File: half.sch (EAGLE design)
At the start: 112 parts, among them IC1 TLC59711, IC2 TLC59711, IC3 TLC59711, IC4 74HC08D, J2 AUDIO_JACK_TRRSCUI, J3 AUDIO_JACK_TRRSCUI, J4 FEMALE 2x3, J5 FEMALE 2x3, SW11 CHERRY-MX-LEDSMD, SW12 CHERRY-MX-LEDSMD, SW13 CHERRY-MX-LEDSMD, SW14 CHERRY-MX-LEDSMD, SW15 CHERRY-MX-LEDSMD, SW16 CHERRY-MX-LEDSMD, SW21 CHERRY-MX-LEDSMD, SW22 CHERRY-MX-LEDSMD, SW23 CHERRY-MX-LEDSMD, SW24 CHERRY-MX-LEDSMD, SW25 CHERRY-MX-LEDSMD, SW26 CHERRY-MX-LEDSMD, SW31 CHERRY-MX-LEDSMD, SW32 CHERRY-MX-LEDSMD, SW33 CHERRY-MX-LEDSMD, SW34 CHERRY-MX-LEDSMD, SW35 CHERRY-MX-LEDSMD, SW36 CHERRY-MX-LEDSMD, SW41 CHERRY-MX-LEDSMD, SW42 CHERRY-MX-LEDSMD, SW43 CHERRY-MX-LEDSMD, SW44 CHERRY-MX-LEDSMD, SW45 CHERRY-MX-LEDSMD, SW46 CHERRY-MX-LEDSMD, SW51 CHERRY-MX-LEDSMD, SW52 CHERRY-MX-LEDSMD, SW53 CHERRY-MX-LEDSMD, SW54 CHERRY-MX-LEDSMD, SW55 CHERRY-MX-LEDSMD, SW56 CHERRY-MX-LEDSMD, U1 MBT40, U2 SPX3819-3.3, U3 MCP73831T-2ACI/OT, U4 32U4, Y1 8MHz

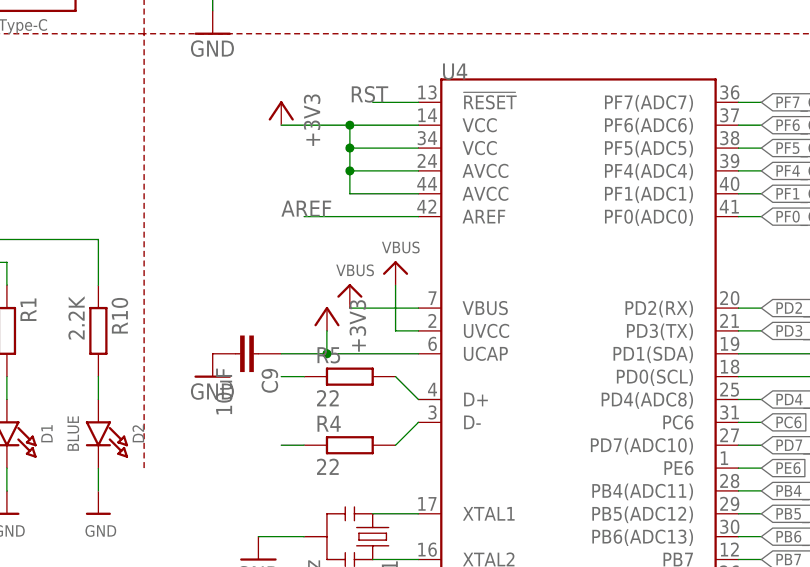
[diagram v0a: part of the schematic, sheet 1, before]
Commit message: Disconnect UVCC on 32u4 to reflect a greenwire fix on PCB
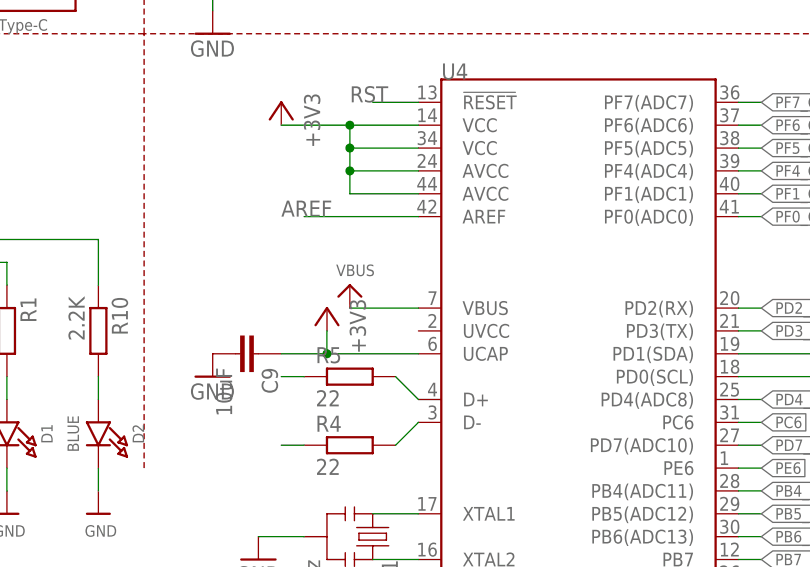
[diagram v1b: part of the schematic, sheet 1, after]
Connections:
- net VBUS: no longer U4.UVCC
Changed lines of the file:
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@@
 <part name="+3V5" library="supply1" deviceset="+3V3" device=""/>
 <part name="U$59" library="microbuilder" deviceset="VBUS" device=""/>
-<part name="U$60" library="microbuilder" deviceset="VBUS" device=""/>
 <part name="GND11" library="supply1" deviceset="GND" device=""/>
 <part name="GND13" library="supply1" deviceset="GND" device=""/>
@@
 <instance part="+3V5" gate="G$1" x="226.06" y="111.76" rot="MR0"/>
 <instance part="U$59" gate="G$1" x="139.7" y="149.86"/>
-<instance part="U$60" gate="G$1" x="162.56" y="63.5"/>
 <instance part="GND11" gate="1" x="208.28" y="134.62"/>
 <instance part="GND13" gate="1" x="208.28" y="157.48"/>
@@
 <junction x="139.7" y="144.78"/>
 </segment>
-<segment>
-<pinref part="U4" gate="U1" pin="UVCC"/>
-<wire x1="165.1" y1="55.88" x2="162.56" y2="55.88" width="0.1524" layer="91"/>
-<wire x1="162.56" y1="55.88" x2="162.56" y2="60.96" width="0.1524" layer="91"/>
-<pinref part="U$60" gate="G$1" pin="VBUS"/>
-</segment>
-</net>
+</net>
